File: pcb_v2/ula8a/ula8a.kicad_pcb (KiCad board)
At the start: 2 copper layers, 174 x 153.7 mm, 81 parts, among them J1 designador, J2 ula_opp, J3 ula_opp, J4 ula_opp, J5 ula_opp, J6 ula_opp, J7 ula_opp, J8 bus_mgrf_1, J9 bus_mgrf_2, Q1 BC548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

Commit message: concluidas as modificações de layout na pcb
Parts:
- U16: footprint Display_7Segment:Sx39-1xxxxx -> 7segdisplay:1-digit-13mm
- moved U16 37.2 mm to (67.9, 161.3)
- moved R2 12.1 mm to (55.2, 111.8), turned to 0 degrees
- moved Q1 8.85 mm to (58.4, 117.2), turned to 180 degrees
- moved D12 0.64 mm to (152.4, 165.7)
- moved D19 0.64 mm to (163.8, 165.7)
- moved D20 0.64 mm to (175.3, 165.7)
- moved R12 0.63 mm to (146.7, 167.0)
- moved R19 0.63 mm to (158.1, 167.0)
- moved R20 0.63 mm to (169.5, 167.0)
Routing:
- net wr_addr_4: track 6.35 -> 179.8 mm, vias 1 -> 2
- net write_enable: track 6.99 -> 178.9 mm, vias 1 -> 2
- net wr_addr_3: track 126.8 -> 295.9 mm
- net wr_addr_0: track 133.5 -> 295.6 mm
- net wr_addr_2: track 139.9 -> 301.7 mm
- net wr_addr_1: track 139.0 -> 297.4 mm
- net rd_addr_2: track 0.00 -> 155.4 mm, vias 0 -> 1
- net rd_addr_3: track 0.00 -> 154.5 mm, vias 0 -> 1
- net rd_addr_4: track 0.00 -> 153.5 mm, vias 0 -> 1
- net overflow_flag_out: track 40.5 -> 192.1 mm, vias 0 -> 5
- net rd_addr_1: track 0.00 -> 146.1 mm, vias 0 -> 1
- net rd_addr_0: track 0.00 -> 145.6 mm, vias 0 -> 1
- net carry_flag_out: track 165.9 -> 279.6 mm, vias 2 -> 3
- net int_mask_in: track 32.1 -> 143.9 mm, vias 1 -> 2
- net data_0: track 84.0 -> 194.9 mm, vias 2 -> 7
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
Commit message: mais alterações na pcb
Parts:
- moved D12 51.7 mm to (190.5, 130.8)
- moved R12 51.7 mm to (184.8, 132.1)
- moved D10 51.3 mm to (152.4, 165.1)
- moved R10 51.3 mm to (146.7, 166.4)
- moved R2 50.2 mm to (83.8, 153.0), turned to 90 degrees
- moved Q1 41.2 mm to (78.7, 153.0), turned to 90 degrees
- moved U15 14.6 mm to (48.9, 121.9)
- moved C15 14.5 mm to (51.5, 118.1)
- moved U16 1.27 mm to (67.9, 160.0)
- moved D14 0.64 mm to (135.9, 165.1)
- moved D15 0.64 mm to (124.5, 165.1)
- moved D16 0.64 mm to (113.0, 165.1)
- moved D19 0.64 mm to (163.8, 165.1)
- moved D20 0.64 mm to (175.3, 165.1)
- moved R14 0.63 mm to (130.2, 166.4)
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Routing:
- net ula_enable: track 288.8 -> 368.4 mm, vias 3 -> 6
- net Net-(Q1-C): track 58.0 -> 19.4 mm
- net +5V: track 626.8 -> 607.8 mm
- net invert_ula_bus: track 295.3 -> 276.6 mm, vias 2 -> 3
- net Net-(U15-e): track 70.3 -> 52.2 mm
- net Net-(U15-f): track 64.5 -> 46.7 mm
- net write_psw: track 237.9 -> 221.1 mm
- net Net-(U15-d): track 63.3 -> 48.4 mm, vias 0 -> 1
- net Net-(U15-g): track 55.2 -> 40.6 mm, vias 2 -> 1
- net Net-(U15-a): track 54.0 -> 39.6 mm, vias 1 -> 0
- net Net-(U15-b): track 57.5 -> 46.2 mm, vias 1 -> 0
- net Net-(U15-c): track 62.1 -> 54.0 mm, vias 1 -> 0
- net write_acc: track 243.2 -> 236.2 mm
- net wr_addr_0: track 295.6 -> 289.3 mm
- net wr_addr_1: track 297.4 -> 292.6 mm
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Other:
- board text added: "SELECT"

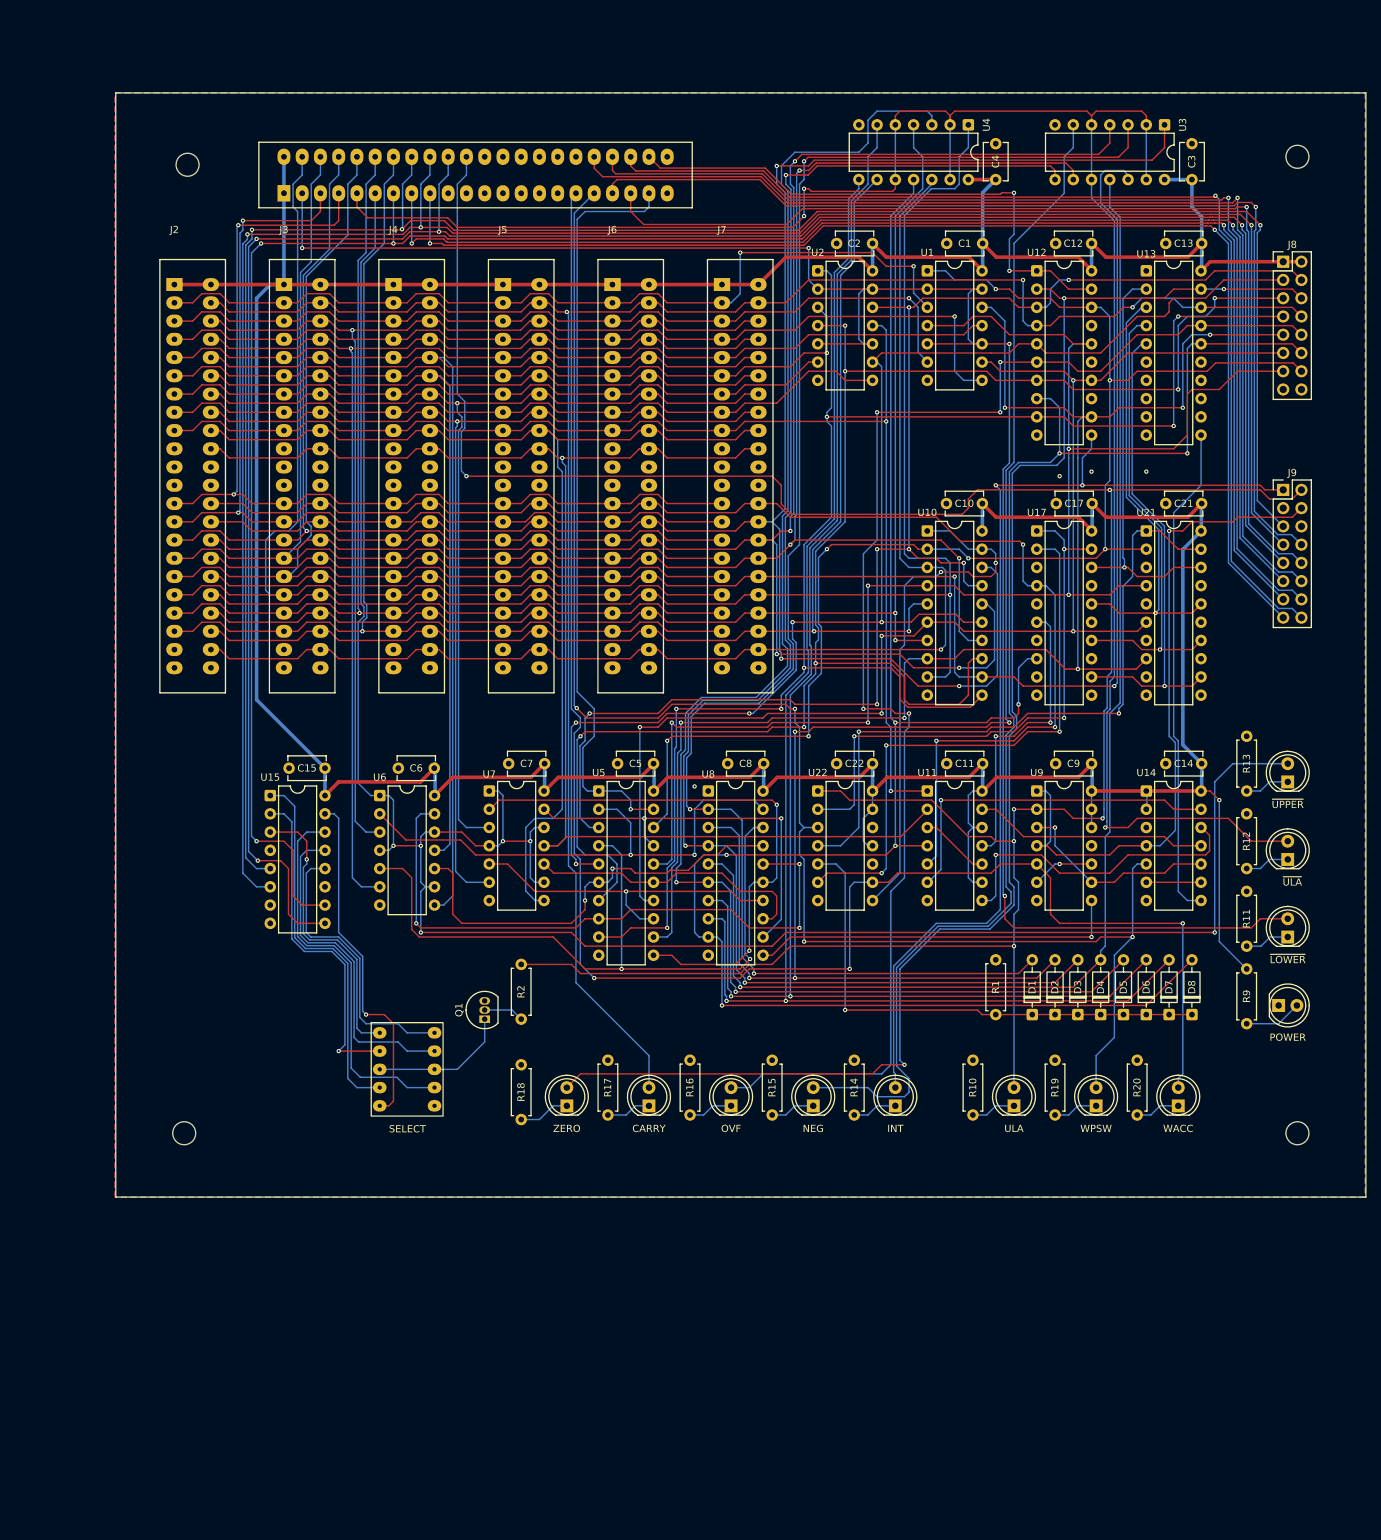
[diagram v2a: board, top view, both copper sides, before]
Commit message: refazendo os pcbs para caber em folha A4
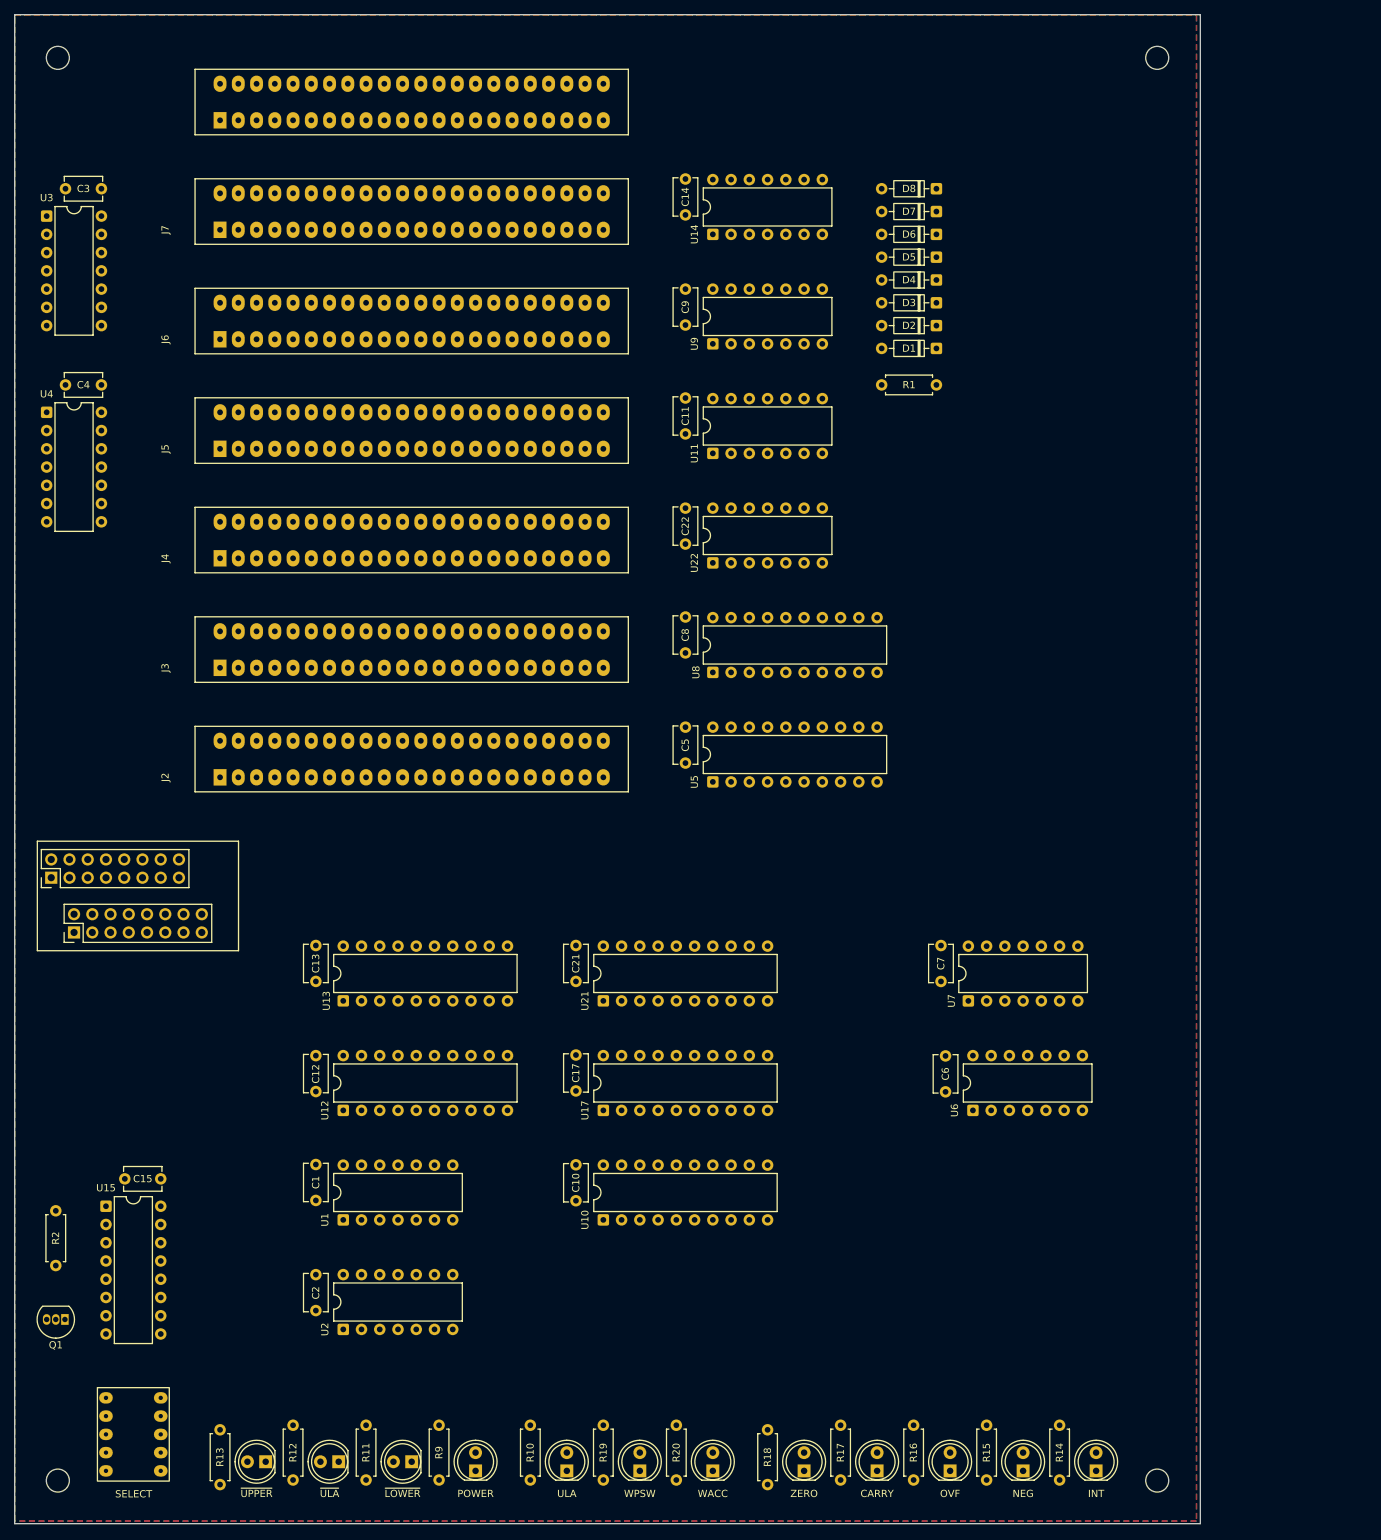
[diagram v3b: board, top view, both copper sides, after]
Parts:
- J8: value bus_mgrf_1 -> sysbus_1
- J9: value bus_mgrf_2 -> sysbus2
- moved J8 191.7 mm to (18.4, 133.3), turned to 90 degrees
- moved J9 179.2 mm to (21.6, 141.0), turned to 90 degrees
- moved R13 172.4 mm to (41.9, 217.8)
- moved D13 170.8 mm to (48.3, 214.6), turned to 180 degrees
- moved C2 165.2 mm to (55.2, 193.6), turned to 90 degrees
- moved U2 161.4 mm to (59.1, 196.2), turned to 90 degrees
- moved C1 159.5 mm to (55.2, 178.3), turned to 90 degrees
- moved C3 156.9 mm to (20.4, 37.5), turned to 0 degrees
- moved C13 156.6 mm to (55.2, 147.8), turned to 90 degrees
- moved C12 156.6 mm to (55.2, 163.1), turned to 90 degrees
- moved D12 156.4 mm to (58.4, 214.6), turned to 180 degrees
- moved U3 156.1 mm to (17.8, 41.3), turned to 0 degrees
- moved U1 155.1 mm to (59.1, 181.0), turned to 90 degrees
- moved R12 153.7 mm to (52.1, 209.6), turned to -90 degrees
- moved U12 151.5 mm to (59.1, 165.7), turned to 90 degrees
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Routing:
- net +5V: track 607.8 -> 0.00 mm, vias 1 -> 0
- net ula_enable: track 368.4 -> 0.00 mm, vias 6 -> 0
- net wr_addr_2: track 303.9 -> 0.00 mm, vias 4 -> 0
- net wr_addr_3: track 297.6 -> 0.00 mm, vias 4 -> 0
- net invert_upper_bus: track 296.8 -> 0.00 mm, vias 6 -> 0
- net wr_addr_1: track 292.6 -> 0.00 mm, vias 3 -> 0
- net wr_addr_0: track 289.3 -> 0.00 mm, vias 3 -> 0
- net carry_flag_out: track 279.6 -> 0.00 mm, vias 3 -> 0
- net invert_ula_bus: track 276.6 -> 0.00 mm, vias 3 -> 0
- net invert_lower_bus: track 268.7 -> 0.00 mm, vias 4 -> 0
- net ula_bus0: track 260.8 -> 0.00 mm, vias 3 -> 0
- net to_acc_7: track 245.8 -> 0.00 mm, vias 5 -> 0
- net ula_bus1: track 244.4 -> 0.00 mm, vias 4 -> 0
- net write_acc: track 236.2 -> 0.00 mm, vias 3 -> 0
- net data_4: track 230.1 -> 0.00 mm, vias 7 -> 0
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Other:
- board size 174 x 153.7 mm -> 165 x 210 mm

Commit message: concluído o layout da pcb
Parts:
- D11: value ~{LOWER} -> LOWER
- D12: value ~{ULA} -> ULA
- D13: value ~{UPPER} -> UPPER
- J2, J3, J4, J5, J6, J7: value ula_opp -> operador
- J8: value sysbus_1 -> bus_mgrf_1
- J9: value sysbus2 -> bus_mgrf_2
- moved C1 165.5 mm to (124.5, 27.9), turned to 0 degrees
- moved U1 161.9 mm to (121.9, 31.8), turned to 0 degrees
- moved U14 128.1 mm to (121.9, 171.4), turned to 0 degrees
- moved C14 127.8 mm to (124.5, 167.6), turned to 0 degrees
- moved C3 127.6 mm to (108.0, 130.2)
- moved U3 127.6 mm to (105.4, 134.0)
- moved C10 126.8 mm to (124.5, 55.9), turned to 0 degrees
- moved U10 124.2 mm to (121.9, 59.7), turned to 0 degrees
- moved U9 112.5 mm to (105.4, 171.4), turned to 0 degrees
- moved C9 111.2 mm to (108.0, 167.6), turned to 0 degrees
- moved U22 108.5 mm to (39.4, 171.4), turned to 0 degrees
- moved C4 108.0 mm to (124.5, 93.3)
- moved U4 108.0 mm to (121.9, 97.2)
- moved C22 103.4 mm to (42.0, 167.6), turned to 0 degrees
- moved U11 99.5 mm to (88.9, 171.4), turned to 0 degrees
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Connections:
- U6 pad 1: invert_upper_bus -> Net-(U5-I0a)
- U6 pad 10: Net-(U5-I2a) -> invert_upper_bus
- U6 pad 12: invert_upper_bus -> Net-(U5-I3a)
- U6 pad 13: Net-(U5-I3a) -> invert_upper_bus
- U6 pad 2: Net-(U5-I0a) -> invert_upper_bus
- U6 pad 3: upper_bus0 -> upper_bus1
- U6 pad 4: invert_upper_bus -> Net-(U5-I1a)
- U6 pad 5: Net-(U5-I1a) -> invert_upper_bus
- U6 pad 6: upper_bus1 -> upper_bus0
- U6 pad 9: invert_upper_bus -> Net-(U5-I2a)
- U7 pad 10: Net-(U5-I2b) -> invert_upper_bus
- U7 pad 9: invert_upper_bus -> Net-(U5-I2b)
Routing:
- net +5V: track 0.00 -> 744.7 mm
- net invert_lower_bus: track 0.00 -> 411.0 mm, vias 0 -> 4
- net invert_ula_bus: track 0.00 -> 346.6 mm, vias 0 -> 7
- net invert_upper_bus: track 0.00 -> 336.9 mm, vias 0 -> 6
- net carry_flag_out: track 0.00 -> 329.4 mm, vias 0 -> 4
- net ula_enable: track 0.00 -> 274.0 mm, vias 0 -> 2
- net data_3: track 0.00 -> 261.5 mm, vias 0 -> 8
- net data_6: track 0.00 -> 255.2 mm, vias 0 -> 4
- net write_psw: track 0.00 -> 253.7 mm, vias 0 -> 6
- net data_2: track 0.00 -> 251.1 mm, vias 0 -> 10
- net data_1: track 0.00 -> 247.6 mm, vias 0 -> 8
- net data_0: track 0.00 -> 244.4 mm, vias 0 -> 5
- net lower_bus7: track 0.00 -> 244.2 mm, vias 0 -> 4
- net data_7: track 0.00 -> 243.4 mm, vias 0 -> 3
- net write_acc: track 0.00 -> 238.1 mm, vias 0 -> 3
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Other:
- board size 165 x 210 mm -> 126.3 x 210 mm
- board text added: "A"
- board text added: "B"
- board text added: "Rev.A1 abril/2026"
- board text added: "ULA8"
- board text added: "bus ula8"

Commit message: inversão na posição dos conectores, para coincidir com o sysbus
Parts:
- D10: value ULA -> ULA SEL
- moved J8 12.7 mm to (21.6, 141.0)
- moved J9 12.7 mm to (21.6, 128.3)
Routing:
- net int_mask_in: track 163.3 -> 187.8 mm, vias 1 -> 3
- net clock: track 136.2 -> 158.8 mm, vias 2 -> 3
- net rd_addr_2: track 82.1 -> 59.9 mm, vias 1 -> 0
- net rd_addr_0: track 87.4 -> 66.4 mm, vias 2 -> 1
- net rd_addr_3: track 78.6 -> 58.4 mm
- net rd_addr_1: track 85.4 -> 65.2 mm, vias 2 -> 1
- net wr_addr_4: track 108.6 -> 93.8 mm, vias 1 -> 2
- net write_enable: track 105.0 -> 93.0 mm, vias 1 -> 3
- net rd_addr_4: track 69.1 -> 59.1 mm, vias 0 -> 1
- net carry_flag_out: track 329.4 -> 321.2 mm, vias 4 -> 3
- net zero_flag_out: track 143.8 -> 150.9 mm, vias 0 -> 2
- net wr_addr_2: track 162.8 -> 156.1 mm, vias 1 -> 2
- net wr_addr_1: track 161.8 -> 155.3 mm, vias 2 -> 3
- net data_1: track 247.6 -> 253.8 mm, vias 8 -> 7
- net data_3: track 261.5 -> 255.3 mm
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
